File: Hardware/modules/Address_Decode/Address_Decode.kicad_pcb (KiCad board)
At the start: 4 copper layers, 83.3 x 68.2 mm, 32 parts, among them J1 Bus_PCI_6502, J2 Clock_Sel, SW1 Manual_Clock, U1 74HC14, U2 74HC00, U3 74LS20, U4 DS1501YZ, U5 74LS393, U6 74HC138, U7 74HC688, X1 8MHz, Y1 G33270007

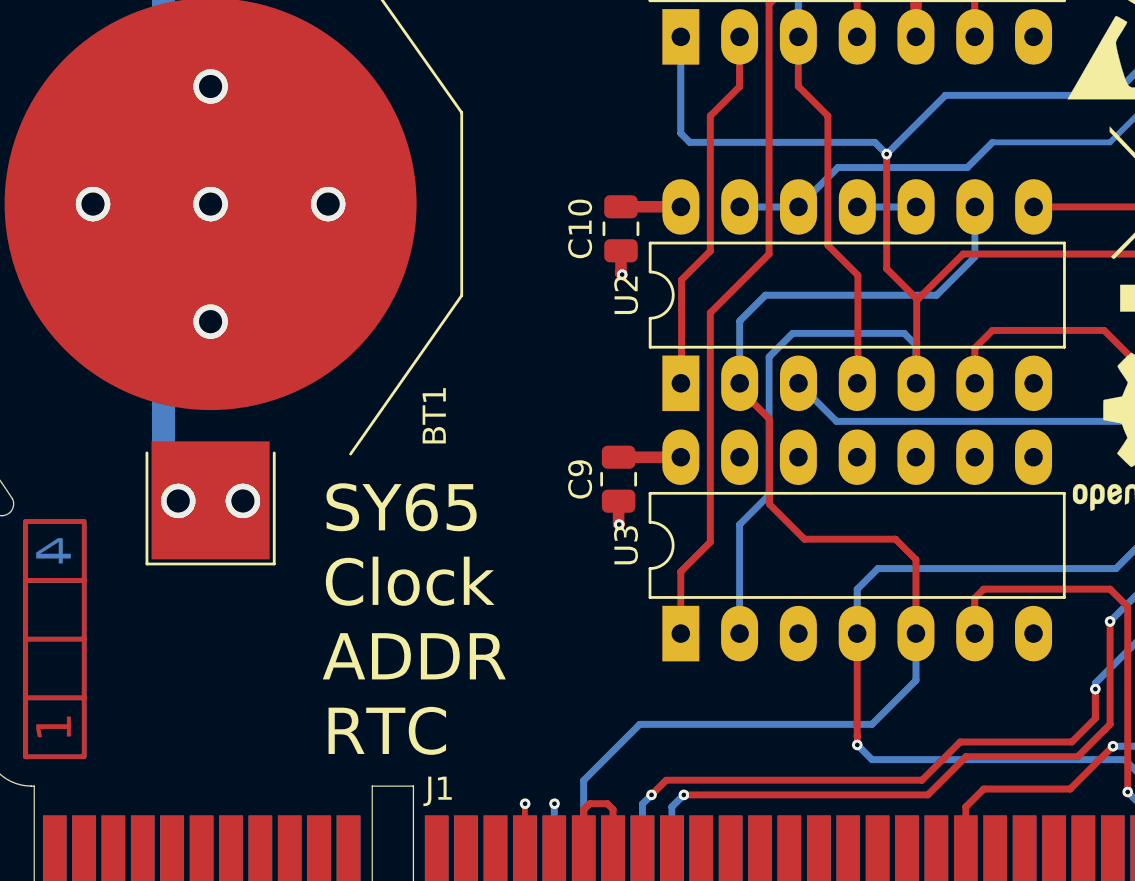
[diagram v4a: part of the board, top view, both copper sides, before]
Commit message: Hardware Review Pt. 1 fix Address Decoding for Strobe Generators add bulk capacitance to every board fix wiring of Prototyping Board
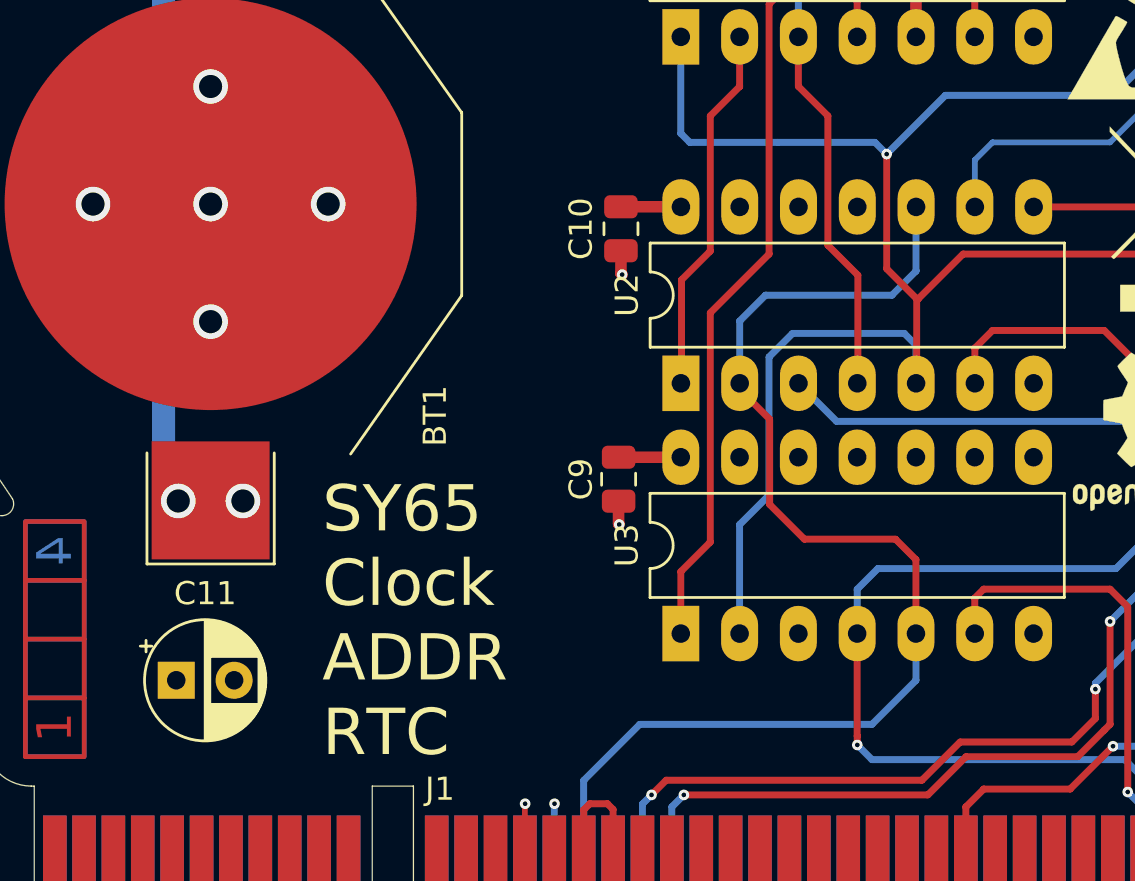
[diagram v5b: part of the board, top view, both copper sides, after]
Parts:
- added C11: 10µ, Capacitor_THT:CP_Radial_D5.0mm_P2.50mm, F.Cu at (138.2, 88.8)
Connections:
- U2 pad 10: Net-(U2-Pad10) -> /CLK
- U2 pad 11: Net-(U2-Pad10) -> unconnected-(U2-Pad11)
- U2 pad 12: /PORT_144 -> GND
- U2 pad 13: /PORT_144 -> GND
- U2 pad 9: /CLK -> /PORT_144
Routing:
- net /PORT_144: track 43.5 -> 34.5 mm
- net Net-(U2-Pad10): track 2.54 -> 0.00 mm
- net /CLK: track 116.4 -> 117.5 mm

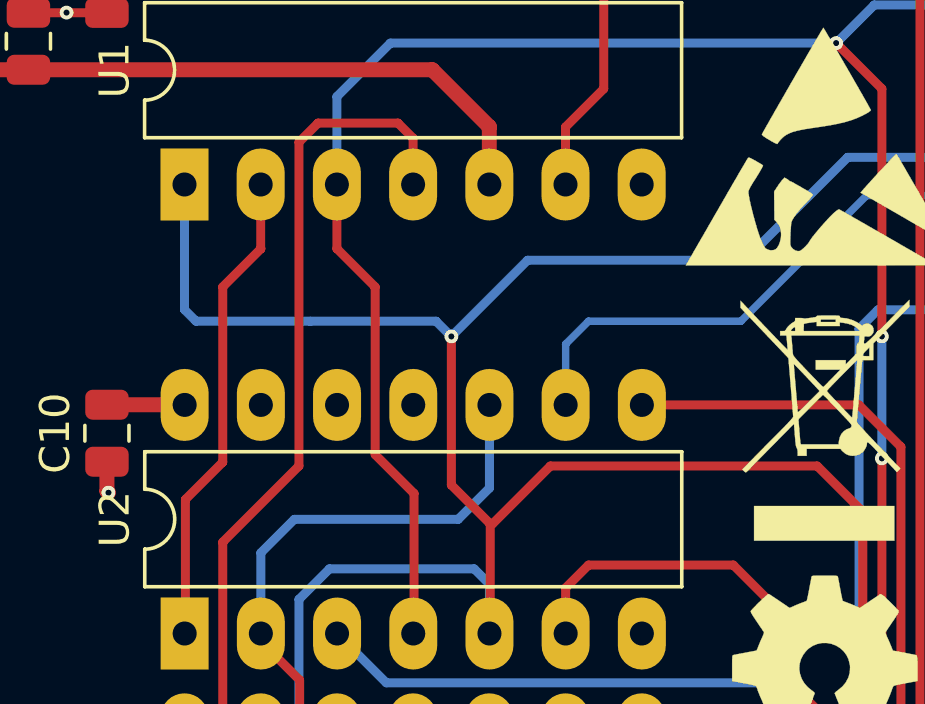
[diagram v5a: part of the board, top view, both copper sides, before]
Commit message: update address decode
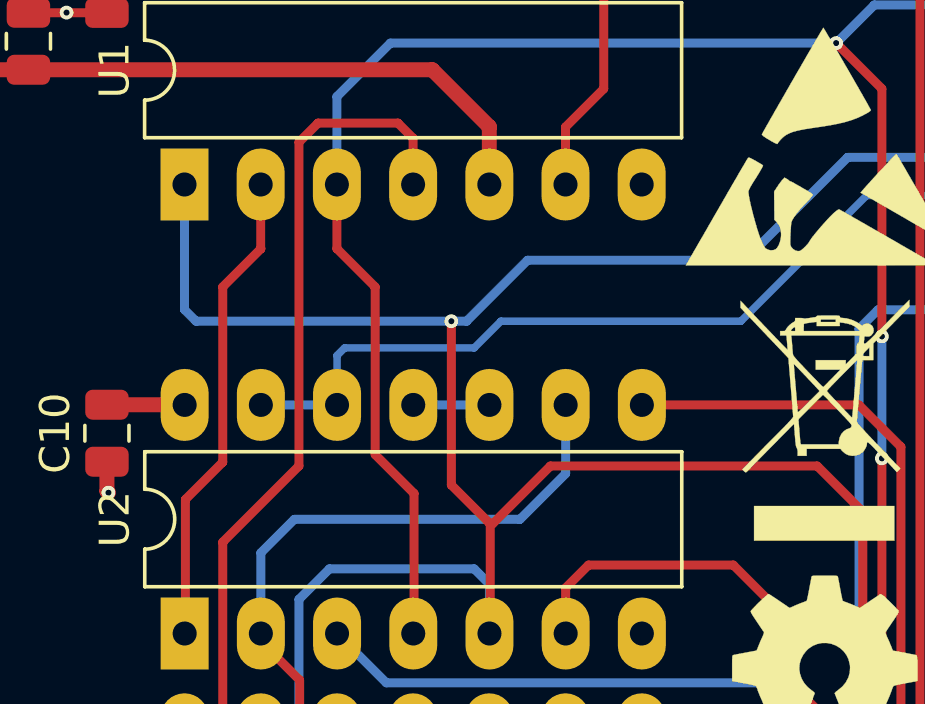
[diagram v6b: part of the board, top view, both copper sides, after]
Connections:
- U2 pad 10: /CLK -> Net-(U2-Pad10)
- U2 pad 11: unconnected-(U2-Pad11) -> Net-(U2-Pad10)
- U2 pad 12: GND -> /PORT_144
- U2 pad 13: GND -> /PORT_144
- U2 pad 9: /PORT_144 -> /CLK
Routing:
- net /PORT_144: track 34.5 -> 44.4 mm
- net Net-(U2-Pad10): track 0.00 -> 2.54 mm
- net /CLK: track 117.5 -> 116.5 mm
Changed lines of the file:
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@@
 	(net 100 "unconnected-(U1-Pad8)")
 	(net 101 "/~{A14}")
-	(net 102 "unconnected-(U2-Pad11)")
+	(net 102 "Net-(U2-Pad10)")
 	(net 103 "Net-(U4-~{CE})")
 	(net 104 "unconnected-(U3-Pad8)")
@@
 			(layers "*.Cu" "*.Mask")
 			(remove_unused_layers no)
-			(net 94 "/PORT_144")
+			(net 22 "/CLK")
 			(pintype "input")
 		)
@@
 			(layers "*.Cu" "*.Mask")
 			(remove_unused_layers no)
-			(net 22 "/CLK")
+			(net 102 "Net-(U2-Pad10)")
 			(pintype "input")
 		)
@@
 			(layers "*.Cu" "*.Mask")
 			(remove_unused_layers no)
-			(net 102 "unconnected-(U2-Pad11)")
-			(pintype "output+no_connect")
+			(net 102 "Net-(U2-Pad10)")
+			(pintype "output")
 		)
 		(pad "12" thru_hole oval
@@
 			(layers "*.Cu" "*.Mask")
 			(remove_unused_layers no)
-			(net 2 "GND")
+			(net 94 "/PORT_144")
 			(pintype "input")
 		)
@@
 			(layers "*.Cu" "*.Mask")
 			(remove_unused_layers no)
-			(net 2 "GND")
+			(net 94 "/PORT_144")
 			(pintype "input")
 		)
@@
 	)
 	(segment
-		(start 172.339 64.643)
-		(end 170.18 66.802)
+		(start 179.197 61.595)
+		(end 172.72 68.072)
 		(width 0.5)
 		(layer "In1.Cu")
@@
 	)
 	(segment
-		(start 176.149 64.643)
-		(end 172.339 64.643)
-		(width 0.5)
-		(layer "In1.Cu")
-		(net 22)
-	)
-	(segment
-		(start 179.197 38.481)
-		(end 179.197 61.595)
-		(width 0.5)
-		(layer "In1.Cu")
-		(net 22)
-	)
-	(segment
 		(start 182.88 37.592)
 		(end 180.086 37.592)
@@
 	)
 	(segment
-		(start 170.18 66.802)
-		(end 170.18 68.3223)
+		(start 172.72 68.072)
+		(end 172.72 68.3223)
 		(width 0.5)
 		(layer "In1.Cu")
@@
 	)
 	(segment
-		(start 179.197 61.595)
-		(end 176.149 64.643)
+		(start 179.197 38.481)
+		(end 179.197 61.595)
 		(width 0.5)
 		(layer "In1.Cu")
@@
 	)
 	(segment
-		(start 208.28 37.592)
-		(end 182.88 37.592)
-		(width 0.5)
+		(start 162.56 75.9423)
+		(end 162.56 73.2528)
+		(width 0.3)
 		(layer "B.Cu")
 		(net 22)
 	)
 	(segment
-		(start 169.1378 72.136)
-		(end 170.18 71.0938)
-		(width 0.3)
+		(start 208.28 37.592)
+		(end 182.88 37.592)
+		(width 0.5)
 		(layer "B.Cu")
 		(net 22)
@@
 	)
 	(segment
-		(start 162.56 73.2528)
-		(end 163.6768 72.136)
+		(start 168.275 90.678)
+		(end 158.242 90.678)
 		(width 0.3)
 		(layer "B.Cu")
@@
 	)
 	(segment
-		(start 168.275 90.678)
-		(end 158.242 90.678)
+		(start 172.72 70.612)
+		(end 172.72 68.3223)
 		(width 0.3)
 		(layer "B.Cu")
@@
 	)
 	(segment
-		(start 163.6768 72.136)
-		(end 169.1378 72.136)
+		(start 162.56 73.2528)
+		(end 163.6768 72.136)
 		(width 0.3)
 		(layer "B.Cu")
@@
 	)
 	(segment
-		(start 170.18 71.0938)
-		(end 170.18 68.3223)
+		(start 163.6768 72.136)
+		(end 171.196 72.136)
 		(width 0.3)
 		(layer "B.Cu")
@@
 	)
 	(segment
-		(start 162.56 75.9423)
-		(end 162.56 73.2528)
+		(start 170.175 86.756)
+		(end 170.175 88.778)
 		(width 0.3)
 		(layer "B.Cu")
@@
 	)
 	(segment
-		(start 170.175 86.756)
-		(end 170.175 88.778)
+		(start 171.196 72.136)
+		(end 172.72 70.612)
 		(width 0.3)
 		(layer "B.Cu")
@@
 	)
 	(segment
-		(start 168.91 70.993)
-		(end 170.2062 72.2892)
+		(start 183.896 86.233)
+		(end 182.626 84.963)
 		(width 0.3)
 		(layer "F.Cu")
@@
 	)
 	(segment
-		(start 183.896 86.233)
-		(end 182.626 84.963)
+		(start 170.2808 72.2892)
+		(end 170.2062 72.2892)
 		(width 0.3)
 		(layer "F.Cu")
@@
 	)
 	(segment
-		(start 170.2808 72.2892)
+		(start 168.91 70.993)
 		(end 170.2062 72.2892)
 		(width 0.3)
@@
 	)
 	(segment
-		(start 168.91 66.04)
+		(start 168.91 65.532)
 		(end 168.91 70.993)
 		(width 0.3)
@@
 	)
 	(via
-		(at 168.91 66.04)
+		(at 168.91 65.532)
 		(size 0.46)
 		(drill 0.2)
@@
 	)
 	(segment
-		(start 160.015 60.975)
-		(end 160.015 65.146)
+		(start 168.91 65.532)
+		(end 169.418 65.532)
 		(width 0.3)
 		(layer "B.Cu")
@@
 	)
 	(segment
-		(start 169.672 73.787)
-		(end 170.18 74.295)
+		(start 160.015 65.146)
+		(end 160.015 60.975)
 		(width 0.3)
 		(layer "B.Cu")
@@
 	)
 	(segment
-		(start 164.846 73.787)
-		(end 169.672 73.787)
+		(start 169.418 65.532)
+		(end 171.45 63.5)
 		(width 0.3)
 		(layer "B.Cu")
@@
 	)
 	(segment
-		(start 162.555 82.047)
-		(end 163.83 80.772)
+		(start 169.672 73.787)
+		(end 170.18 74.295)
 		(width 0.3)
 		(layer "B.Cu")
@@
 	)
 	(segment
-		(start 171.45 63.5)
-		(end 178.689 63.5)
+		(start 164.846 73.787)
+		(end 169.672 73.787)
 		(width 0.3)
 		(layer "B.Cu")
@@
 	)
 	(segment
-		(start 163.83 74.803)
-		(end 164.846 73.787)
+		(start 182.118 60.071)
+		(end 187.325 60.071)
 		(width 0.3)
 		(layer "B.Cu")
@@
 	)
 	(segment
-		(start 178.689 63.5)
-		(end 182.118 60.071)
+		(start 162.555 82.047)
+		(end 163.83 80.772)
 		(width 0.3)
 		(layer "B.Cu")
@@
 	)
 	(segment
-		(start 168.402 65.532)
-		(end 168.91 66.04)
+		(start 168.91 65.532)
+		(end 160.401 65.532)
 		(width 0.3)
 		(layer "B.Cu")
@@
 	)
 	(segment
-		(start 160.015 65.146)
-		(end 160.401 65.532)
+		(start 163.83 74.803)
+		(end 164.846 73.787)
 		(width 0.3)
 		(layer "B.Cu")
@@
 	)
 	(segment
-		(start 160.401 65.532)
-		(end 164.211 65.532)
+		(start 171.45 63.5)
+		(end 178.689 63.5)
 		(width 0.3)
 		(layer "B.Cu")
@@
 	)
 	(segment
-		(start 182.118 60.071)
-		(end 187.325 60.071)
+		(start 160.401 65.532)
+		(end 160.015 65.146)
 		(width 0.3)
 		(layer "B.Cu")
@@
 	)
 	(segment
-		(start 164.211 65.532)
-		(end 168.402 65.532)
-		(width 0.3)
-		(layer "B.Cu")
-		(net 70)
-	)
-	(segment
-		(start 168.91 66.04)
-		(end 171.45 63.5)
+		(start 178.689 63.5)
+		(end 182.118 60.071)
 		(width 0.3)
 		(layer "B.Cu")
@@
 	)
 	(segment
+		(start 170.561 65.532)
+		(end 169.672 66.421)
+		(width 0.25)
+		(layer "B.Cu")
+		(net 94)
+	)
+	(segment
 		(start 200.787 57.531)
 		(end 198.247 60.071)
@@
 	)
 	(segment
-		(start 178.562 65.532)
-		(end 173.482 65.532)
+		(start 196.977 61.341)
+		(end 182.753 61.341)
 		(width 0.25)
 		(layer "B.Cu")
@@
 	)
 	(segment
-		(start 173.482 65.532)
-		(end 172.72 66.294)
+		(start 178.562 65.532)
+		(end 170.561 65.532)
 		(width 0.25)
 		(layer "B.Cu")
@@
 	)
 	(segment
-		(start 182.753 61.341)
-		(end 178.562 65.532)
+		(start 165.1 66.675)
+		(end 165.1 68.3223)
 		(width 0.25)
 		(layer "B.Cu")
@@
 	)
 	(segment
-		(start 172.72 66.294)
-		(end 172.72 68.3223)
-		(width 0.25)
+		(start 162.56 68.3223)
+		(end 165.1 68.3223)
+		(width 0.3)
 		(layer "B.Cu")
 		(net 94)
@@
 	)
 	(segment
-		(start 196.977 61.341)
-		(end 182.753 61.341)
+		(start 169.672 66.421)
+		(end 165.354 66.421)
+		(width 0.25)
+		(layer "B.Cu")
+		(net 94)
+	)
+	(segment
+		(start 182.753 61.341)
+		(end 178.562 65.532)
+		(width 0.25)
+		(layer "B.Cu")
+		(net 94)
+	)
+	(segment
+		(start 165.354 66.421)
+		(end 165.1 66.675)
 		(width 0.25)
 		(layer "B.Cu")
@@
 	)
 	(segment
+		(start 170.18 68.3223)
+		(end 167.64 68.3223)
+		(width 0.3)
+		(layer "B.Cu")
+		(net 102)
+	)
+	(segment

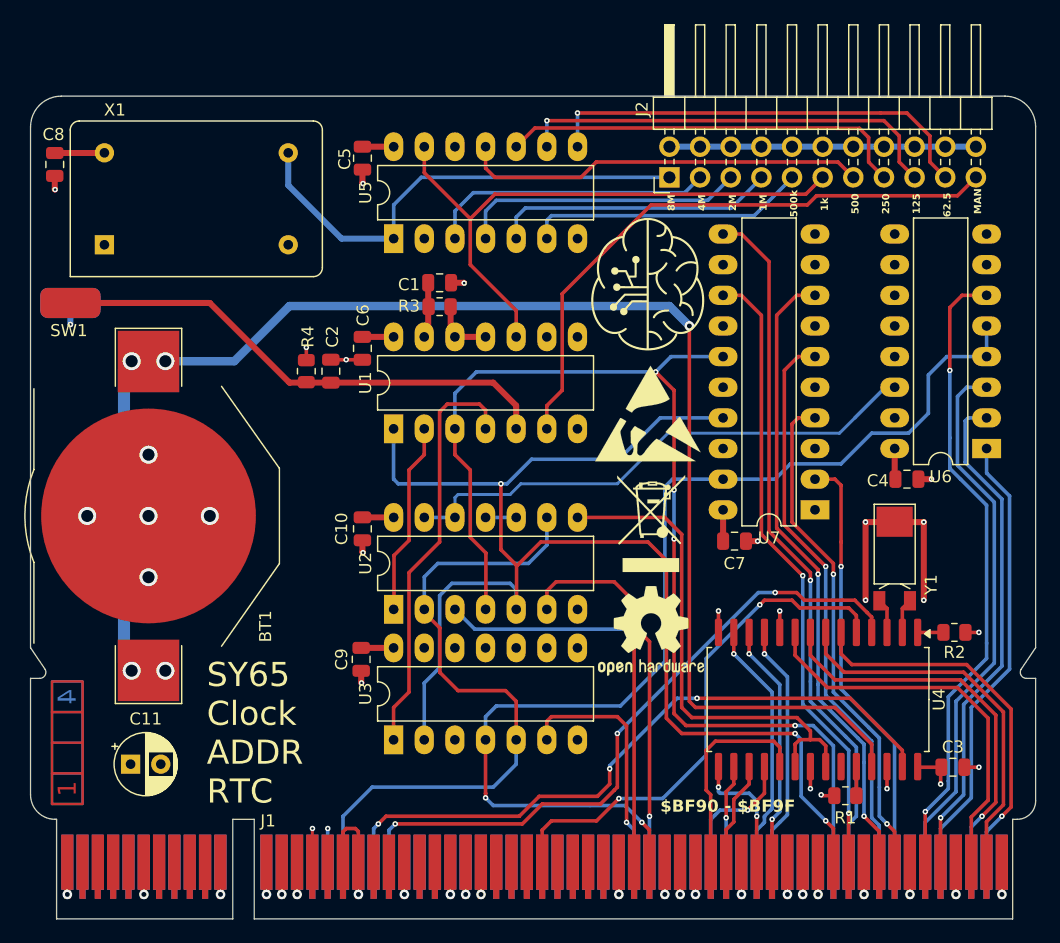
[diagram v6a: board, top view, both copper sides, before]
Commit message: Big Review Update - Changed Copper Pours on all PCBs - Implemented errors found at review - fixed some additional errors
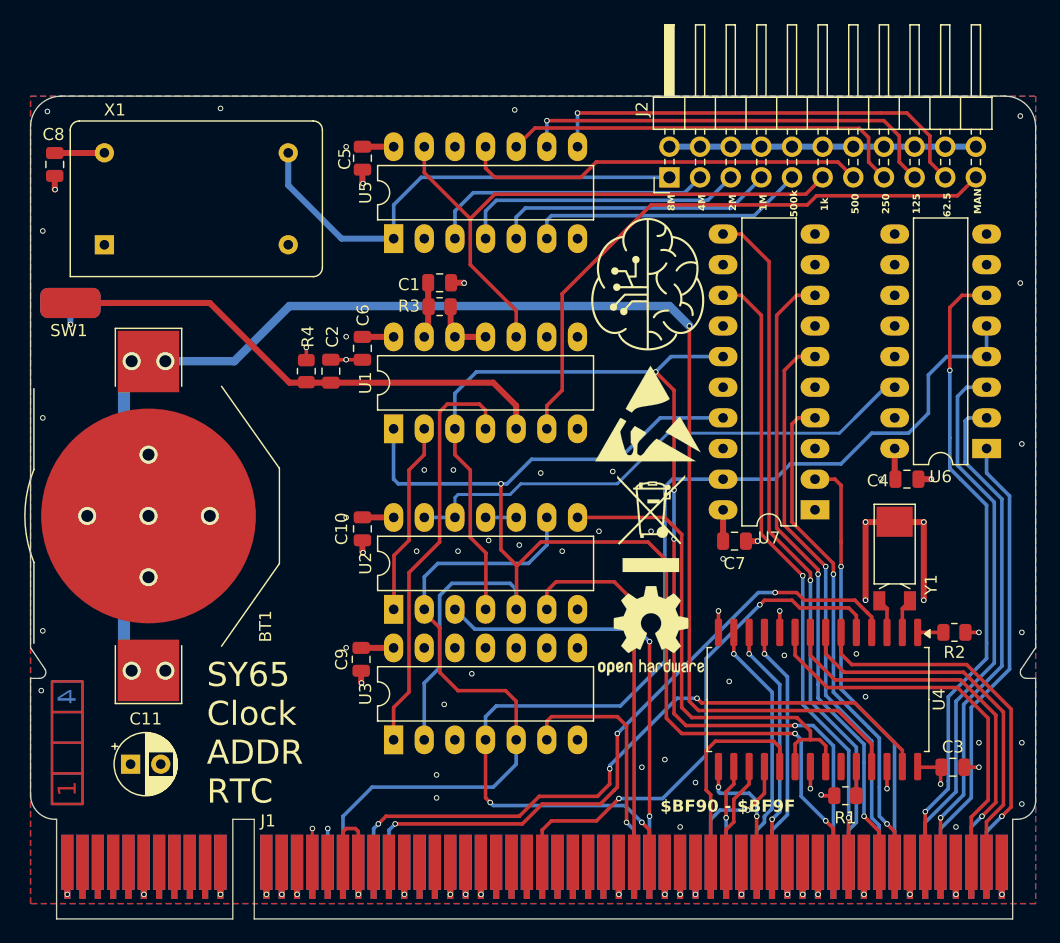
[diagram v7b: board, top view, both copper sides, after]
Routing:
- net +5V: vias 8 -> 52
- added copper zone on B.Cu, net +5V
- added copper zone on F.Cu, net +5V
- removed copper zone on In1.Cu, net +5V
